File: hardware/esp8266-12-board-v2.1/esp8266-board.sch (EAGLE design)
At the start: 24 parts, among them T1 AMS1117, T2 LM7805

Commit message: just after notebook crash
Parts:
- added ENABLE_WATCHDOG: PIN-HEADER-2PIN, stutz-components-library:PIN-HEADER-2PIN
- added R10: 10k, stutz-components-library:RESISTORV1
- C3: device capacitor-wima:C2.5/2 -> rcl:CPOL-EUE2,5-6E; MPN 1C10Z5U104M050B -> (none)
- C4: device capacitor-wima:C2.5/2 -> rcl:CPOL-EUE2,5-6E
- FIRMWARE: value GND DTR RTS -> GND DTR RTS RX TX; device stutz-eagle:PIN-HEADER-3PIN -> stutz-components-library:PIN-HEADER-5PIN
- OUTPUT: value GND GND 3.3V 5V RX TX -> PIN-HEADER-5PIN; device stutz-eagle:PIN-HEADER-6PIN -> stutz-components-library:PIN-HEADER-5PIN
- R1, R2, R3, R4, R5, R6, R7, R8: device stutz-eagle:RESISTORV1 -> stutz-components-library:RESISTORV1
- T2: device stutz-eagle:LM7805 -> stutz-components-library:LM7805
- W1: value TPS3823 -> TPS3823-33; device stutz-eagle:TPS382X -> stutz-components-library:STWD100
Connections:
- removed net SD_MISO: E1.MISO, R7.1, SD1.7
- removed net SD_MOSI: E1.MOSI, R6.1, SD1.2
- removed net SD_SCK: E1.SCLK, R8.1, SD1.5
- new net ESP_GPIO12: E1.GPIO12, R7.1, SD1.7
- new net ESP_GPIO13: E1.GPIO13, R6.1, SD1.2
- new net ESP_GPIO14: E1.GPIO14, R8.1, SD1.5
- new net ESP_GPIO16: E1.GPIO16, ENABLE_WATCHDOG.1
- new net ESP_GPIO4: E1.GPIO4, R10.1, SD1.1
- new net ESP_GPIO5: E1.GPIO5
- new net N$1: ENABLE_WATCHDOG.2, W1.WDI
- net +3.3V: now also C4.+, OUTPUT.2, R10.2, W1.EN; no longer C4.1, OUTPUT.3, W1.MR
- net +5V: now also C3.+, OUTPUT.3; no longer C3.1, OUTPUT.4
- net ESP_CH_PD: now also W1.WDO; no longer W1.RESET
- net ESP_GPIO0: no longer W1.WDI
- net ESP_GPIO2: no longer SD1.1
- net ESP_RX: now also FIRMWARE.4, OUTPUT.4; no longer OUTPUT.5
- net ESP_TX: now also FIRMWARE.5, OUTPUT.5; no longer OUTPUT.6
- net GND: now also C3.-, C4.-; no longer C3.2, C4.2, OUTPUT.2
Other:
- note added: "OUTPUT"
- note removed: "GPIO OUTPUT"
- note removed: "SD_CS"
- moved on the sheet: R6

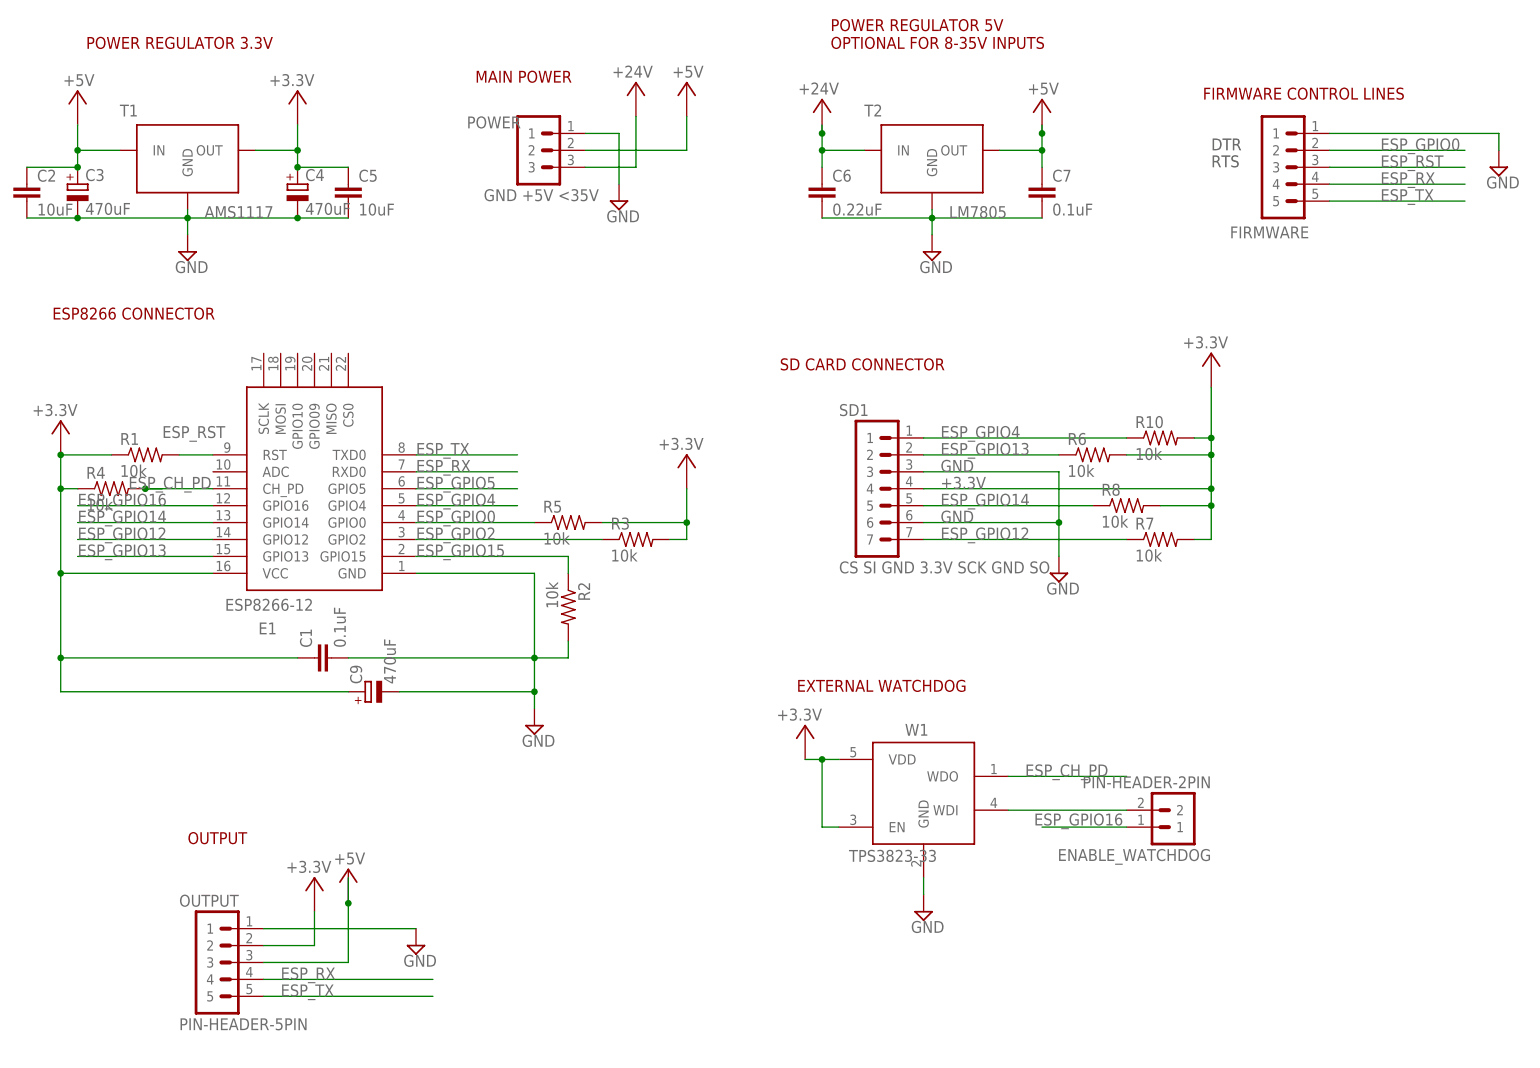
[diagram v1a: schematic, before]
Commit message: Added watchdog from maxim
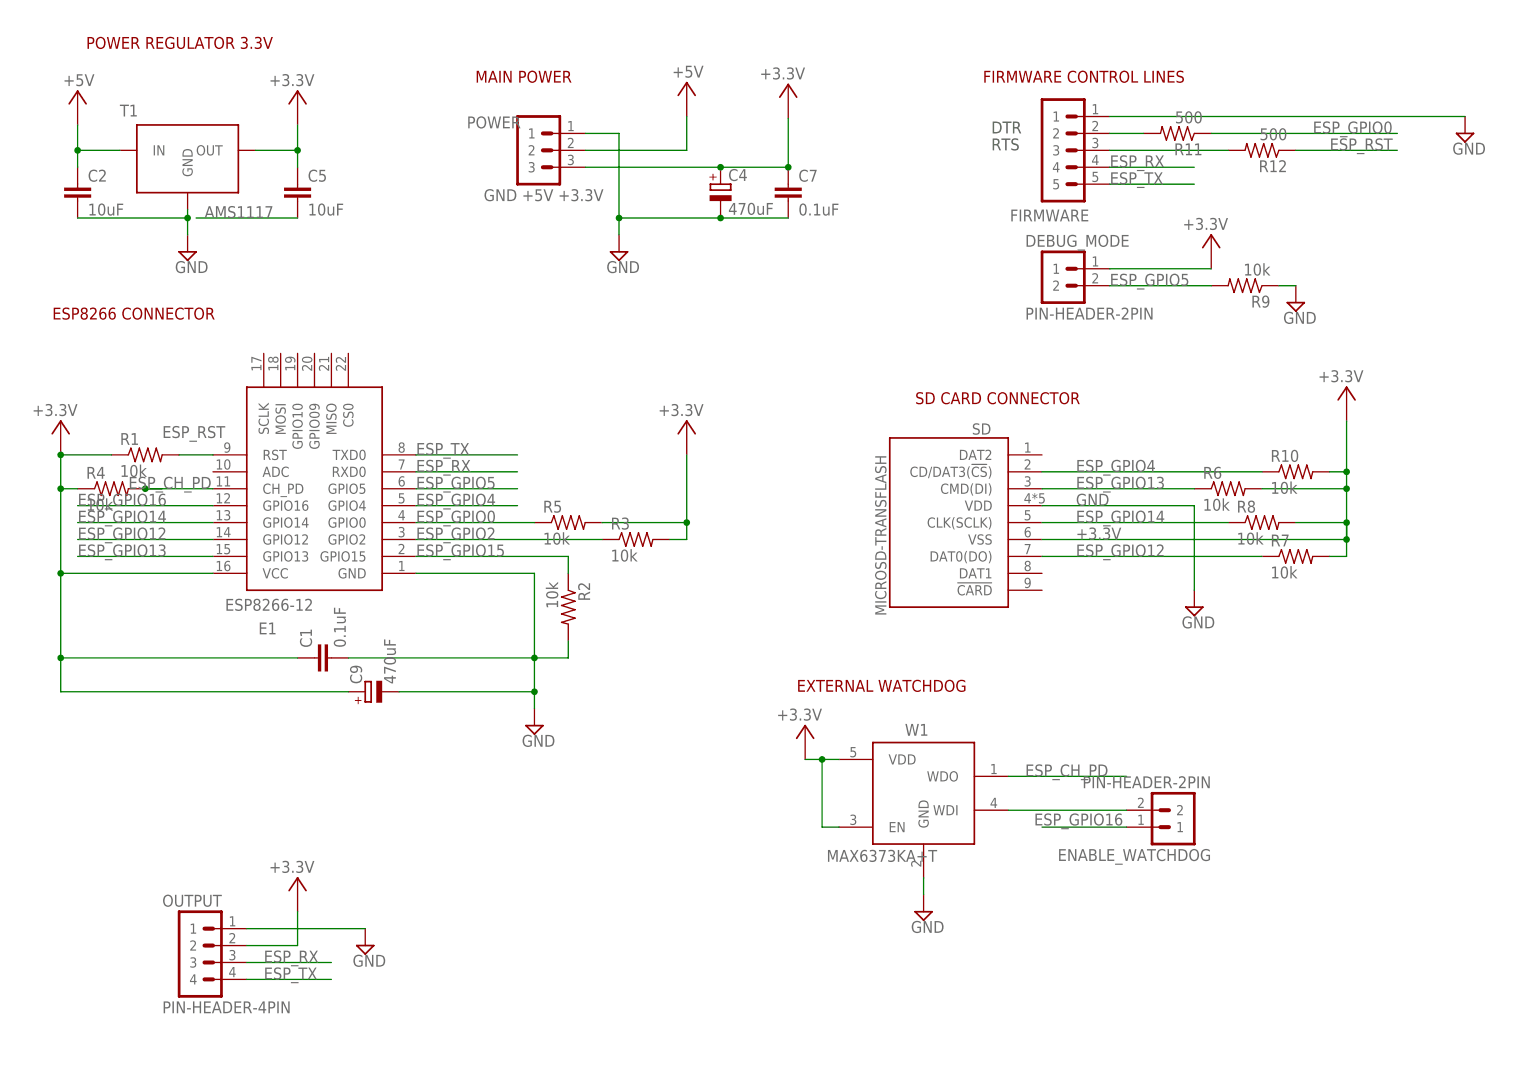
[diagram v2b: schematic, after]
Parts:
- removed C3: 470uF, rcl:CPOL-EUE2,5-6E
- removed C6: 0.22uF, capacitor-wima:C2.5/2
- removed SD1: CS SI GND 3.3V SCK GND SO, stutz-eagle:PIN-HEADER-7PIN
- removed T2: LM7805, stutz-components-library:LM7805
- added DEBUG_MODE: PIN-HEADER-2PIN, stutz-components-library:PIN-HEADER-2PIN
- added R11, R12: 500, stutz-components-library:RESISTORV1
- added R9: 10k, stutz-components-library:RESISTORV1
- added SD: MICROSD-TRANSFLASH, stutz-components-library:MICROSD-TRANSFLASH
- OUTPUT: value PIN-HEADER-5PIN -> PIN-HEADER-4PIN; device stutz-components-library:PIN-HEADER-5PIN -> stutz-components-library:PIN-HEADER-4PIN
- POWER: value GND +5V <35V -> GND +5V +3.3V
- W1: value TPS3823-33 -> MAX6373KA+T
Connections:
- removed net +24V: C6.1, POWER.3, T2.IN
- new net N$6: C5.2
- new net N$7: FIRMWARE.2, R11.2
- new net N$8: FIRMWARE.3, R12.2
- net +3.3V: now also C7.1, DEBUG_MODE.1, POWER.3, SD.VSS; no longer OUTPUT.2, SD1.4
- net +5V: no longer C3.+, C7.1, OUTPUT.3, T2.OUT
- net ESP_GPIO0: now also R11.1; no longer FIRMWARE.2
- net ESP_GPIO12: now also SD.DAT0(DO); no longer SD1.7
- net ESP_GPIO13: now also SD.CMD(DI); no longer SD1.2
- net ESP_GPIO14: now also SD.CLK(SCLK); no longer SD1.5
- net ESP_GPIO4: now also SD.CD/DAT3(!CS!); no longer SD1.1
- net ESP_GPIO5: now also DEBUG_MODE.2, R9.2
- net ESP_RST: now also R12.1; no longer FIRMWARE.3
- net ESP_RX: no longer OUTPUT.4
- net ESP_TX: no longer OUTPUT.5
- net GND: now also R9.1, SD.VDD; no longer C3.-, C5.2, C6.2, OUTPUT.1, SD1.3, SD1.6, T2.GND
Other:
- note removed: "OUTPUT"
- note removed: "POWER REGULATOR 5V OPTIONAL FOR 8-35V INPUTS"
- moved on the sheet: C2, C4, C5, C7, FIRMWARE, R10, R6, R7, R8

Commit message: Updating board for SMD usage
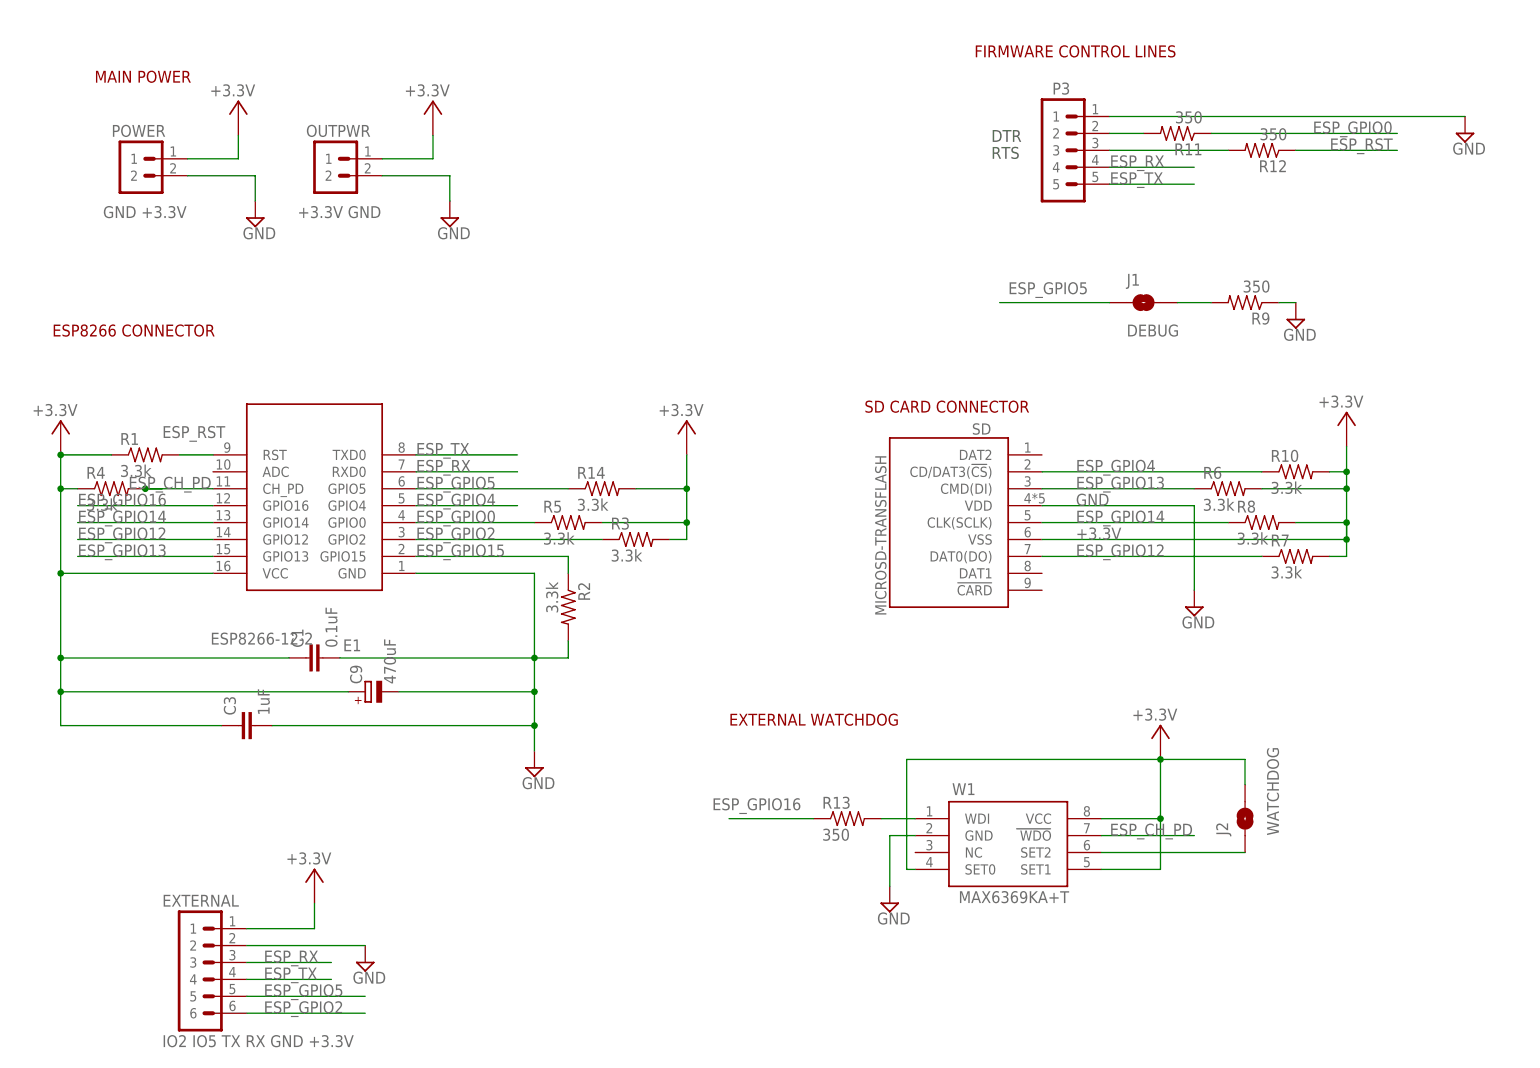
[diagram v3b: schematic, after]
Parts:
- removed C2, C5: 10uF, capacitor-wima:C2.5/2
- removed C4: 470uF, rcl:CPOL-EUE2,5-6E
- removed C7: 0.1uF, capacitor-wima:C2.5/2
- removed DEBUG_MODE, ENABLE_WATCHDOG: PIN-HEADER-2PIN, stutz-components-library:PIN-HEADER-2PIN
- removed OUTPUT: PIN-HEADER-4PIN, stutz-components-library:PIN-HEADER-4PIN
- removed T1: AMS1117, stutz-eagle:AMS1117
- added C3: 1uF, stutz-components-library:CAPACITOR0805
- added EXTERNAL: IO2 IO5 TX RX GND +3.3V, stutz-components-library:PIN-HEADER-6PIN
- added J1: DEBUG, stutz-components-library:JUMPER-PAD-2ROUND
- added J2: WATCHDOG, stutz-components-library:JUMPER-PAD-2ROUND
- added OUTPWR: +3.3V GND, stutz-components-library:PIN-HEADER-2PIN
- added R13: 350, stutz-components-library:RESISTOR0805
- added R14: 3.3k, stutz-components-library:RESISTOR0805
- C1: device capacitor-wima:C2.5/2 -> stutz-components-library:CAPACITOR0805
- E1: value ESP8266-12 -> ESP8266-12-2; device stutz-eagle:ESP8266-12 -> stutz-components-library:ESP8266-12-2
- P3: value GND DTR RTS RX TX -> GND DTR RTS RX TX
- POWER: value GND +5V +3.3V -> GND +3.3V; device stutz-eagle:PIN-HEADER-3PIN -> stutz-components-library:PIN-HEADER-2PIN
- R1, R10, R2, R3, R4, R5, R6, R7, R8: value 10k -> 3.3k; device stutz-components-library:RESISTORV1 -> stutz-components-library:RESISTOR0805
- R11, R12: value 500 -> 350; device stutz-components-library:RESISTORV1 -> stutz-components-library:RESISTOR0805
- R9: value 10k -> 350; device stutz-components-library:RESISTORV1 -> stutz-components-library:RESISTOR0805
- W1: value MAX6373KA+T -> MAX6369KA+T; device stutz-components-library:STWD100 -> stutz-components-library:MAX6369-74
- renumbered FIRMWARE to P3
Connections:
- removed net +5V: C2.1, POWER.2, T1.IN
- new net N$10: R13.2, W1.WDI
- net +3.3V: now also C3.1, EXTERNAL.1, J2.2, OUTPWR.1, POWER.1, R14.2, W1.SET0, W1.SET1, W1.VCC; no longer C4.+, C5.1, C7.1, DEBUG_MODE.1, POWER.3, T1.OUT, W1.EN, W1.VDD
- net ESP_GPIO16: now also R13.1; no longer ENABLE_WATCHDOG.1
- net ESP_GPIO2: now also EXTERNAL.6
- net ESP_GPIO5: now also EXTERNAL.5, J1.1, R14.1; no longer DEBUG_MODE.2, R9.2
- net ESP_RX: now also EXTERNAL.3
- net ESP_TX: now also EXTERNAL.4
- net GND: now also C3.2, EXTERNAL.2, OUTPWR.2, POWER.2; no longer C2.2, C4.-, C7.2, POWER.1, T1.GND
- net N$1: now also J2.1, W1.SET2; no longer ENABLE_WATCHDOG.2, W1.WDI
- net N$6: now also J1.2, R9.2; no longer C5.2
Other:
- note removed: "POWER REGULATOR 3.3V"
- moved on the sheet: C1, R9
